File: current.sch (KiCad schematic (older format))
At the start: 33 parts

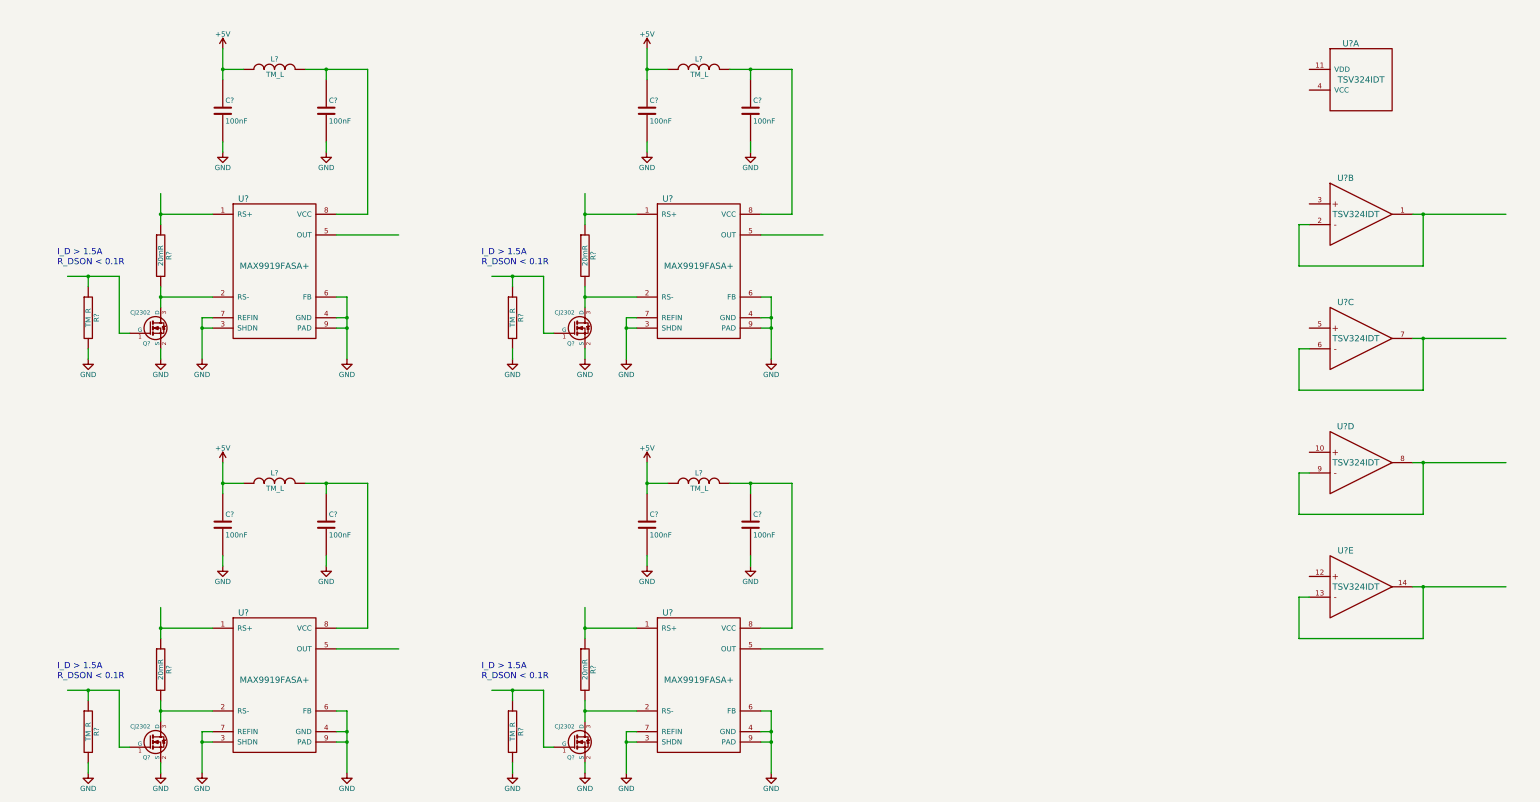
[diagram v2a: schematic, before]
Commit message: resistor network
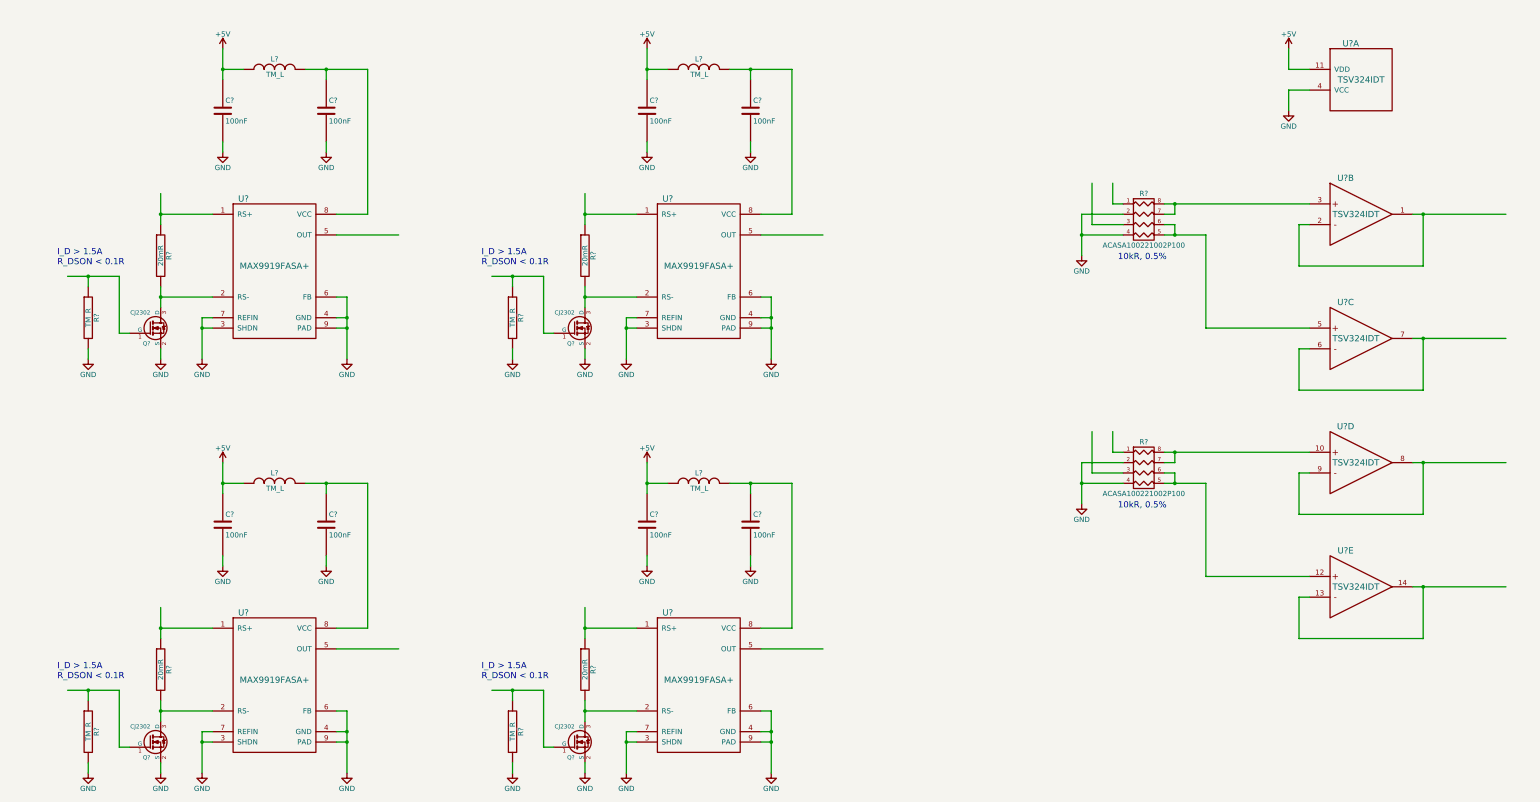
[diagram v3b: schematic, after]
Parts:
- added R? (x2): ACASA100221002P100, symbol R_PACK4
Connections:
- wire segments 160 -> 158
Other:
- note added: "10kR, 0.5%"
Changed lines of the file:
@@
 	7200 4000 6700 4000
 Wire Wire Line
-	6700 3900 6700 4000
-Wire Wire Line
-	6700 4000 6700 4100
+	6700 3900 6700 4100
 Wire Wire Line
 	6700 3200 7200 3200
 Wire Wire Line
-	6700 3000 6700 3200
-Wire Wire Line
-	6700 3200 6700 3300
+	6700 3000 6700 3300
 $Comp
 L TM_C C?
@@
 $EndComp
 Wire Wire Line
-	8500 4000 8500 4200
-Wire Wire Line
-	8500 4200 8500 4300
-Wire Wire Line
-	8500 4300 8500 4600
+	8500 4000 8500 4600
 Wire Wire Line
 	8400 4200 8500 4200
@@
 	7200 4200 7100 4200
 Wire Wire Line
-	7100 4200 7100 4300
-Wire Wire Line
-	7100 4300 7100 4600
+	7100 4200 7100 4600
 Wire Wire Line
 	7200 4300 7100 4300
@@
 $EndComp
 Wire Wire Line
-	7300 1600 7300 1800
-Wire Wire Line
-	7300 1800 7300 1900
+	7300 1600 7300 1900
 $Comp
 L TM_C C?
@@
 	8300 2600 8300 2500
 Wire Wire Line
-	8100 1800 8300 1800
-Wire Wire Line
-	8300 1800 8700 1800
+	8100 1800 8700 1800
 Connection ~ 8300 1800
 Connection ~ 6700 4000
@@
 	6400 4350 6300 4350
 Wire Wire Line
-	6300 4350 6300 3800
-Wire Wire Line
-	6300 3800 6000 3800
-Wire Wire Line
-	6000 3800 5800 3800
+	6300 3800 6300 4350
+Wire Wire Line
+	5800 3800 6300 3800
 $Comp
 L TM_R R?
@@
 	3100 4000 2600 4000
 Wire Wire Line
-	2600 3900 2600 4000
-Wire Wire Line
-	2600 4000 2600 4100
+	2600 3900 2600 4100
 Wire Wire Line
 	2600 3200 3100 3200
 Wire Wire Line
-	2600 3000 2600 3200
-Wire Wire Line
-	2600 3200 2600 3300
+	2600 3000 2600 3300
 $Comp
 L TM_C C?
@@
 $EndComp
 Wire Wire Line
-	4400 4000 4400 4200
-Wire Wire Line
-	4400 4200 4400 4300
-Wire Wire Line
-	4400 4300 4400 4600
+	4400 4000 4400 4600
 Wire Wire Line
 	4300 4200 4400 4200
@@
 	3100 4200 3000 4200
 Wire Wire Line
-	3000 4200 3000 4300
-Wire Wire Line
-	3000 4300 3000 4600
+	3000 4200 3000 4600
 Wire Wire Line
 	3100 4300 3000 4300
@@
 $EndComp
 Wire Wire Line
-	3200 1600 3200 1800
-Wire Wire Line
-	3200 1800 3200 1900
+	3200 1600 3200 1900
 $Comp
 L TM_C C?
@@
 	4200 2600 4200 2500
 Wire Wire Line
-	4000 1800 4200 1800
-Wire Wire Line
-	4200 1800 4600 1800
+	4000 1800 4600 1800
 Connection ~ 4200 1800
 Connection ~ 2600 4000
@@
 	2300 4350 2200 4350
 Wire Wire Line
-	2200 4350 2200 3800
-Wire Wire Line
-	2200 3800 1900 3800
-Wire Wire Line
-	1900 3800 1700 3800
+	2200 3800 2200 4350
+Wire Wire Line
+	1700 3800 2200 3800
 $Comp
 L TM_R R?
@@
 	3100 8000 2600 8000
 Wire Wire Line
-	2600 7900 2600 8000
-Wire Wire Line
-	2600 8000 2600 8100
+	2600 7900 2600 8100
 Wire Wire Line
 	2600 7200 3100 7200
 Wire Wire Line
-	2600 7000 2600 7200
-Wire Wire Line
-	2600 7200 2600 7300
+	2600 7000 2600 7300
 $Comp
 L TM_C C?
@@
 $EndComp
 Wire Wire Line
-	4400 8000 4400 8200
-Wire Wire Line
-	4400 8200 4400 8300
-Wire Wire Line
-	4400 8300 4400 8600
+	4400 8000 4400 8600
 Wire Wire Line
 	4300 8200 4400 8200
@@
 	3100 8200 3000 8200
 Wire Wire Line
-	3000 8200 3000 8300
-Wire Wire Line
-	3000 8300 3000 8600
+	3000 8200 3000 8600
 Wire Wire Line
 	3100 8300 3000 8300
@@
 $EndComp
 Wire Wire Line
-	3200 5600 3200 5800
-Wire Wire Line
-	3200 5800 3200 5900
+	3200 5600 3200 5900
 $Comp
 L TM_C C?
@@
 	4200 6600 4200 6500
 Wire Wire Line
-	4000 5800 4200 5800
-Wire Wire Line
-	4200 5800 4600 5800
+	4000 5800 4600 5800
 Connection ~ 4200 5800
 Connection ~ 2600 8000
@@
 	2300 8350 2200 8350
 Wire Wire Line
-	2200 8350 2200 7800
-Wire Wire Line
-	2200 7800 1900 7800
-Wire Wire Line
-	1900 7800 1700 7800
+	2200 7800 2200 8350
+Wire Wire Line
+	1700 7800 2200 7800
 $Comp
 L TM_R R?
@@
 	7200 8000 6700 8000
 Wire Wire Line
-	6700 7900 6700 8000
-Wire Wire Line
-	6700 8000 6700 8100
+	6700 7900 6700 8100
 Wire Wire Line
 	6700 7200 7200 7200
 Wire Wire Line
-	6700 7000 6700 7200
-Wire Wire Line
-	6700 7200 6700 7300
+	6700 7000 6700 7300
 $Comp
 L TM_C C?
@@
 $EndComp
 Wire Wire Line
-	8500 8000 8500 8200
-Wire Wire Line
-	8500 8200 8500 8300
-Wire Wire Line
-	8500 8300 8500 8600
+	8500 8000 8500 8600
 Wire Wire Line
 	8400 8200 8500 8200
@@
 	7200 8200 7100 8200
 Wire Wire Line
-	7100 8200 7100 8300
-Wire Wire Line
-	7100 8300 7100 8600
+	7100 8200 7100 8600
 Wire Wire Line
 	7200 8300 7100 8300
@@
 $EndComp
 Wire Wire Line
-	7300 5600 7300 5800
-Wire Wire Line
-	7300 5800 7300 5900
+	7300 5600 7300 5900
 $Comp
 L TM_C C?
@@
 	8300 6600 8300 6500
 Wire Wire Line
-	8100 5800 8300 5800
-Wire Wire Line
-	8300 5800 8700 5800
+	8100 5800 8700 5800
 Connection ~ 8300 5800
 Connection ~ 6700 8000
@@
 	6400 8350 6300 8350
 Wire Wire Line
-	6300 8350 6300 7800
-Wire Wire Line
-	6300 7800 6000 7800
-Wire Wire Line
-	6000 7800 5800 7800
+	6300 7800 6300 8350
+Wire Wire Line
+	5800 7800 6300 7800
 $Comp
 L TM_R R?
@@
 	14800 4900 14800 4400
 Wire Wire Line
-	14700 4400 14800 4400
-Wire Wire Line
-	14800 4400 15600 4400
+	14700 4400 15600 4400
 Connection ~ 14800 4400
 Wire Wire Line
@@
 	14800 3700 14800 3200
 Wire Wire Line
-	14700 3200 14800 3200
-Wire Wire Line
-	14800 3200 15600 3200
+	14700 3200 15600 3200
 Connection ~ 14800 3200
 Wire Wire Line
@@
 	14800 7300 14800 6800
 Wire Wire Line
-	14700 6800 14800 6800
-Wire Wire Line
-	14800 6800 15600 6800
+	14700 6800 15600 6800
 Connection ~ 14800 6800
 Wire Wire Line
@@
 	14800 6100 14800 5600
 Wire Wire Line
-	14700 5600 14800 5600
-Wire Wire Line
-	14800 5600 15600 5600
+	14700 5600 15600 5600
 Connection ~ 14800 5600
 Wire Wire Line
@@
 Wire Wire Line
 	13600 6900 13600 7300
+$Comp
+L R_PACK4 R?
+U 1 1 553B9EAA
+P 12100 3450
+F 0 "R?" H 12100 3900 50  0000 C CNN
+F 1 "ACASA100221002P100" H 12100 3400 50  0000 C CNN
+F 2 "" H 12100 3450 60  0000 C CNN
+F 3 "http://www.vishay.com/docs/28754/acaprof.pdf" H 12100 3450 60  0001 C CNN
+	1    12100 3450
+	1    0    0    -1
+$EndComp
+Text Notes 11850 3650 0    60   ~ 0
+10kR, 0.5%
+Wire Wire Line
+	12300 3100 13700 3100
+Wire Wire Line
+	12400 3100 12400 3200
+Wire Wire Line
+	12400 3200 12300 3200
+Wire Wire Line
+	12300 3400 12700 3400
+Wire Wire Line
+	11900 3400 11500 3400
+Wire Wire Line
+	11500 3200 11500 3600
+$Comp
+L GND #PWR?
+U 1 1 553BAC20
+P 11500 3600
+F 0 "#PWR?" H 11500 3350 50  0001 C CNN
+F 1 "GND" H 11500 3450 50  0000 C CNN
+F 2 "" H 11500 3600 60  0000 C CNN
+F 3 "" H 11500 3600 60  0000 C CNN
+	1    11500 3600
+	1    0    0    -1
+$EndComp
+Wire Wire Line
+	11900 3200 11500 3200
+Connection ~ 11500 3400
+Wire Wire Line
+	11900 3100 11800 3100
+Wire Wire Line
+	11800 3100 11800 2900
+Wire Wire Line
+	11900 3300 11600 3300
+Wire Wire Line
+	11600 3300 11600 2900
+Connection ~ 12400 3100
+Wire Wire Line
+	12700 3400 12700 4300
+Wire Wire Line
+	12700 4300 13700 4300
+Connection ~ 12400 3400
+Wire Wire Line
+	12300 3300 12400 3300
+Wire Wire Line
+	12400 3300 12400 3400
+$Comp
+L R_PACK4 R?
+U 1 1 553BBA95
+P 12100 5850
+F 0 "R?" H 12100 6300 50  0000 C CNN
+F 1 "ACASA100221002P100" H 12100 5800 50  0000 C CNN
+F 2 "" H 12100 5850 60  0000 C CNN
+F 3 "http://www.vishay.com/docs/28754/acaprof.pdf" H 12100 5850 60  0001 C CNN
+	1    12100 5850
+	1    0    0    -1
+$EndComp
+Text Notes 11850 6050 0    60   ~ 0
+10kR, 0.5%
+Wire Wire Line
+	12300 5500 13700 5500
+Wire Wire Line
+	12400 5500 12400 5600
+Wire Wire Line
+	12400 5600 12300 5600
+Wire Wire Line
+	12300 5800 12700 5800
+Wire Wire Line
+	11900 5800 11500 5800
+Wire Wire Line
+	11500 5600 11500 6000
+$Comp
+L GND #PWR?
+U 1 1 553BBAA2
+P 11500 6000
+F 0 "#PWR?" H 11500 5750 50  0001 C CNN
+F 1 "GND" H 11500 5850 50  0000 C CNN
+F 2 "" H 11500 6000 60  0000 C CNN
+F 3 "" H 11500 6000 60  0000 C CNN
+	1    11500 6000
+	1    0    0    -1
+$EndComp
+Wire Wire Line
+	11900 5600 11500 5600
+Connection ~ 11500 5800
+Wire Wire Line
+	11900 5500 11800 5500
+Wire Wire Line
+	11800 5500 11800 5300
+Wire Wire Line
+	11900 5700 11600 5700
+Wire Wire Line
+	11600 5700 11600 5300
+Connection ~ 12400 5500
+Wire Wire Line
+	12700 5800 12700 6700
+Wire Wire Line
+	12700 6700 13700 6700
+Connection ~ 12400 5800
+Wire Wire Line
+	12300 5700 12400 5700
+Wire Wire Line
+	12400 5700 12400 5800
+Wire Wire Line
+	13500 2000 13500 2200
+$Comp
+L GND #PWR?
+U 1 1 553BBB87
+P 13500 2200
+F 0 "#PWR?" H 13500 1950 50  0001 C CNN
+F 1 "GND" H 13500 2050 50  0000 C CNN
+F 2 "" H 13500 2200 60  0000 C CNN
+F 3 "" H 13500 2200 60  0000 C CNN
+	1    13500 2200
+	1    0    0    -1
+$EndComp
+Wire Wire Line
+	13700 2000 13500 2000
+$Comp
+L +5V #PWR?
+U 1 1 553BC74B
+P 13500 1600
+F 0 "#PWR?" H 13500 1450 50  0001 C CNN
+F 1 "+5V" H 13500 1740 50  0000 C CNN
+F 2 "" H 13500 1600 60  0000 C CNN
+F 3 "" H 13500 1600 60  0000 C CNN
+	1    13500 1600
+	1    0    0    -1
+$EndComp
+Wire Wire Line
+	13500 1600 13500 1800
+Wire Wire Line
+	13500 1800 13700 1800
 $EndSCHEMATC

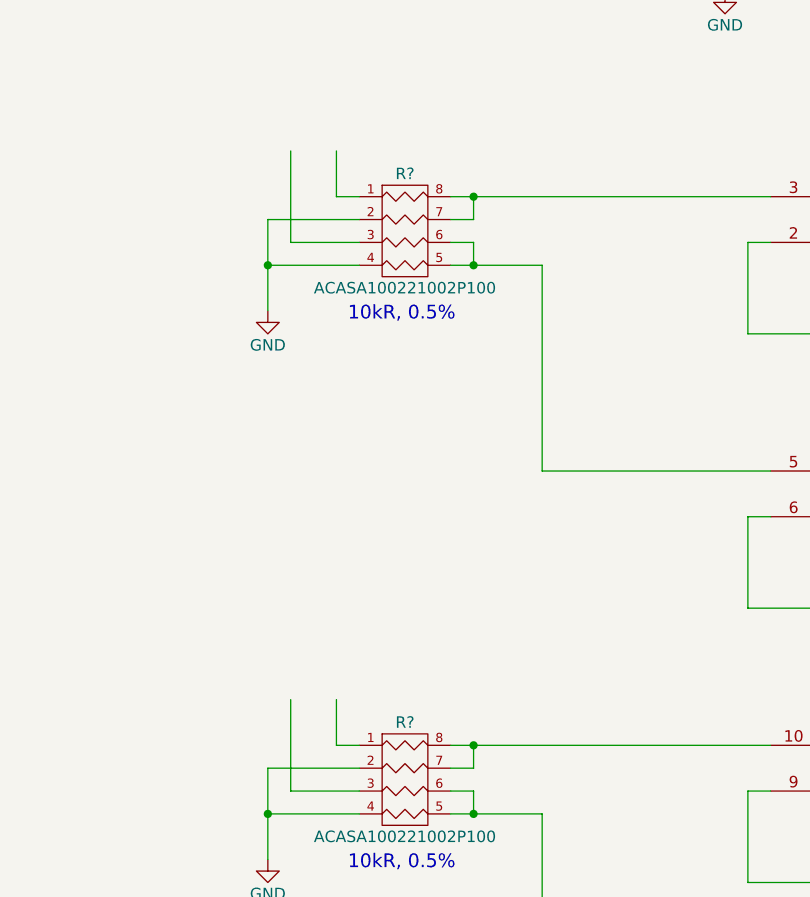
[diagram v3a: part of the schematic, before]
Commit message: resistor network = RN
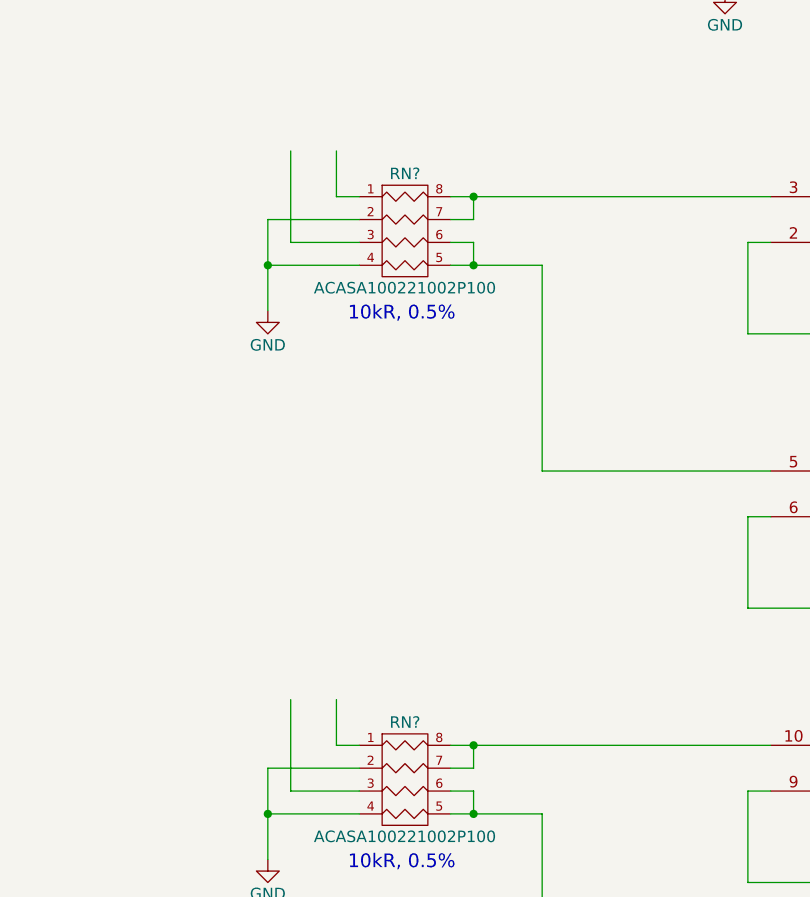
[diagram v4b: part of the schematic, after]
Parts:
- gave numbers to parts that had none: 1
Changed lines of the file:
@@
 	13600 6900 13600 7300
 $Comp
-L R_PACK4 R?
+L R_PACK4 RN?
 U 1 1 553B9EAA
 P 12100 3450
-F 0 "R?" H 12100 3900 50  0000 C CNN
+F 0 "RN?" H 12100 3900 50  0000 C CNN
 F 1 "ACASA100221002P100" H 12100 3400 50  0000 C CNN
 F 2 "" H 12100 3450 60  0000 C CNN
@@
 	12400 3300 12400 3400
 $Comp
-L R_PACK4 R?
+L R_PACK4 RN?
 U 1 1 553BBA95
 P 12100 5850
-F 0 "R?" H 12100 6300 50  0000 C CNN
+F 0 "RN?" H 12100 6300 50  0000 C CNN
 F 1 "ACASA100221002P100" H 12100 5800 50  0000 C CNN
 F 2 "" H 12100 5850 60  0000 C CNN
